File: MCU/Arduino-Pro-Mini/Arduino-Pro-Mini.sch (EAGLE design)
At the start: 19 parts, among them Q1 8/16/20MHz, U1 ATMEGA328

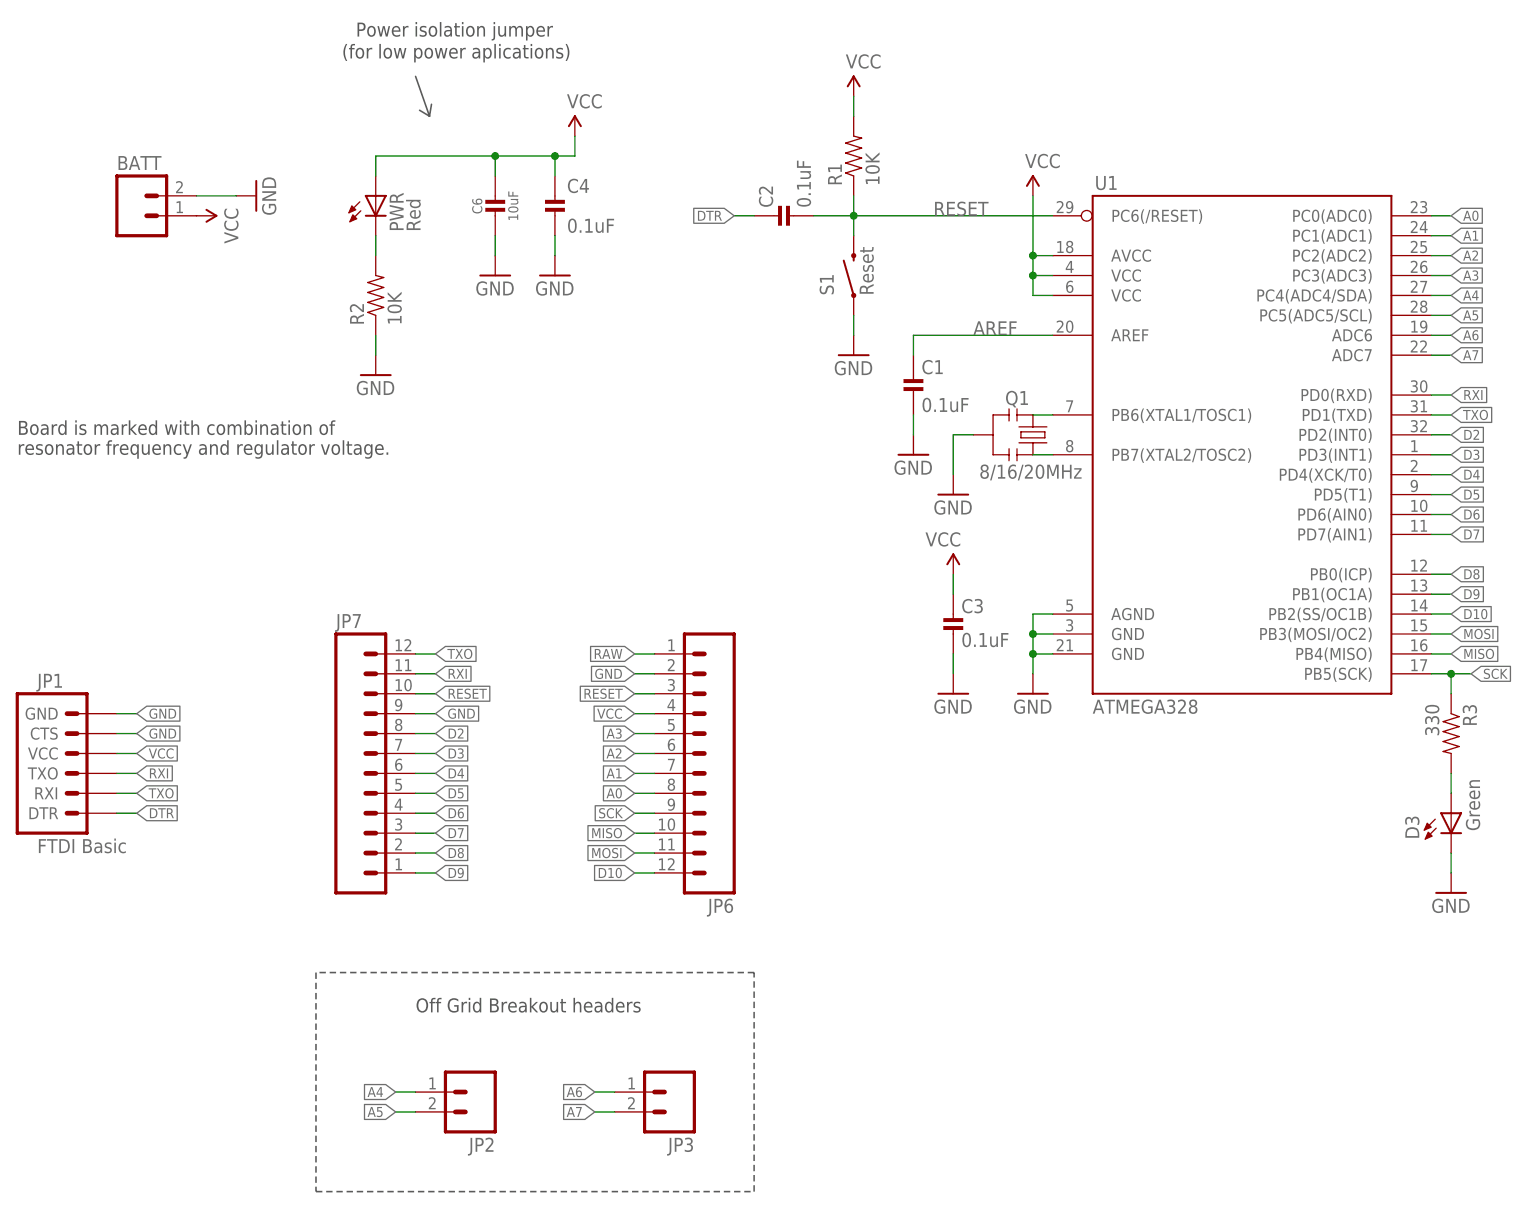
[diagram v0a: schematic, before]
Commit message: pro mini board route
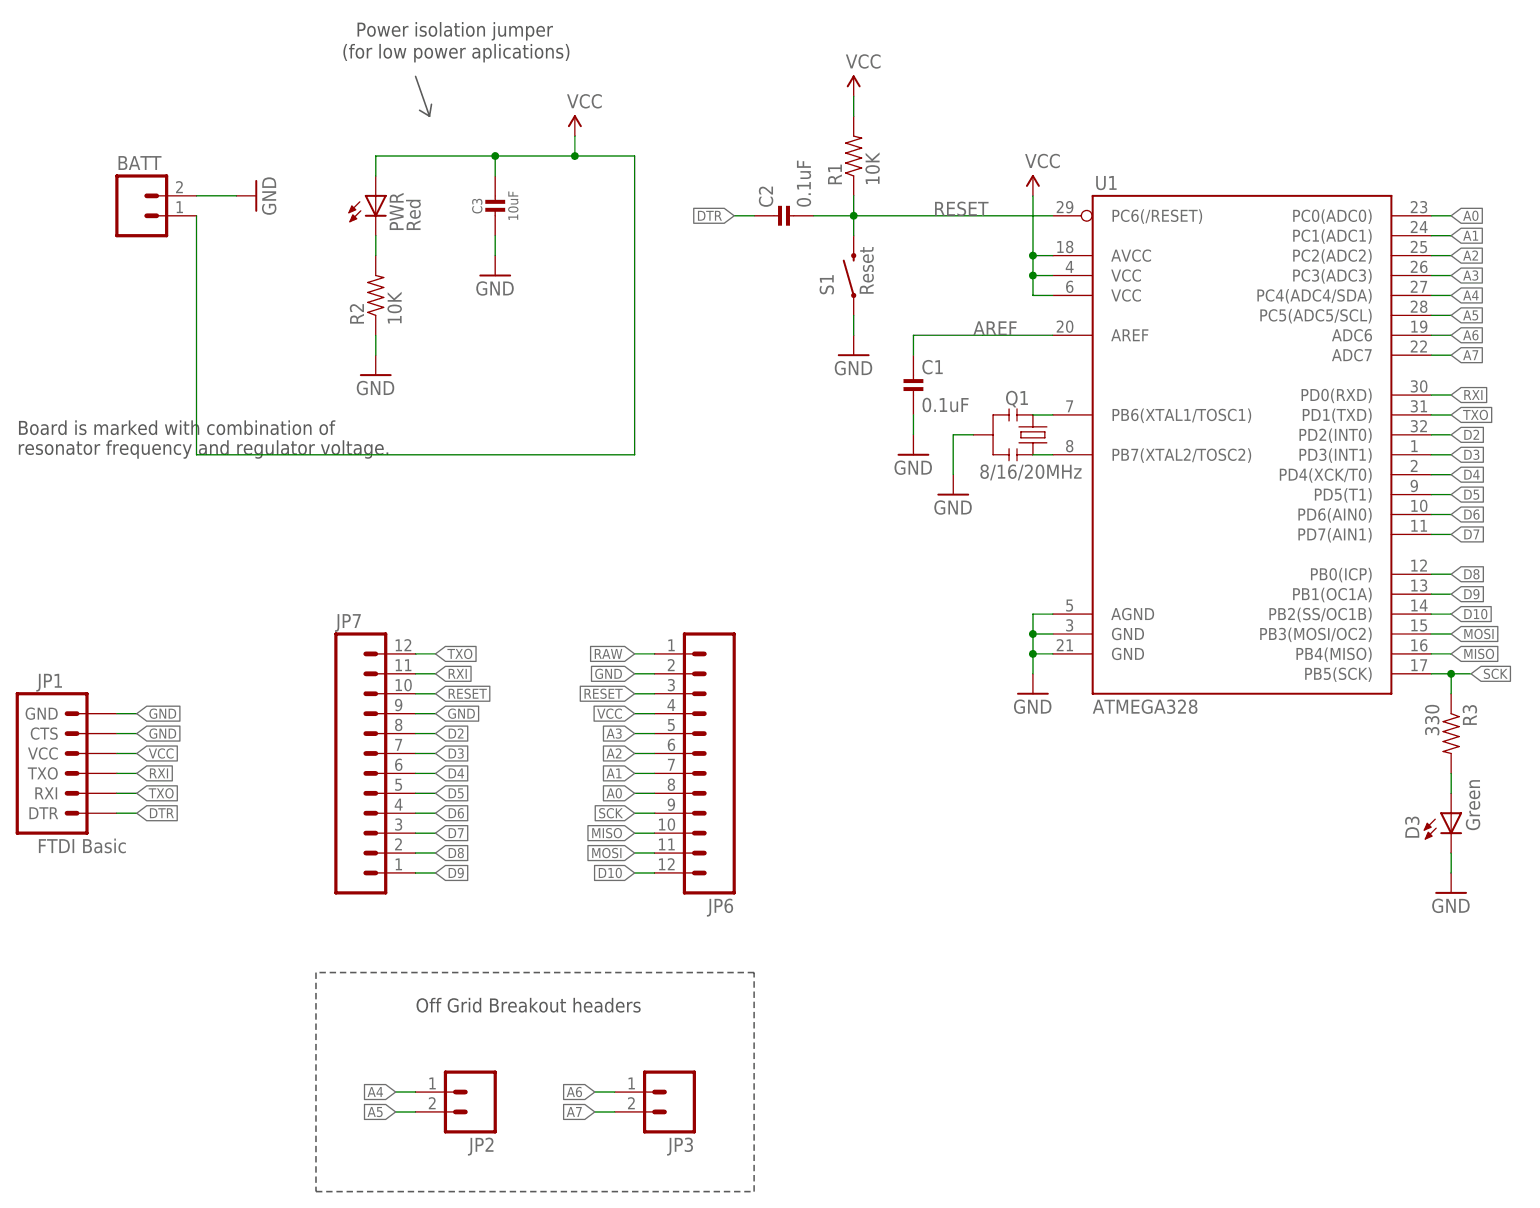
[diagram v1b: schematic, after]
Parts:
- removed C4: 0.1uF, Scott-Electrical:CAP_CERAMIC_0603
- removed C6: 10uF, Scott-Electrical:CAP_CERAMIC_0805
- C3: value 0.1uF -> 10uF; device Scott-Electrical:CAP_CERAMIC_0603 -> Scott-Electrical:CAP_CERAMIC_0805
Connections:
- removed net 3.3V: BATT.1
- net GND: now also C3.2; no longer C3.1, C4.2, C6.2
- net VCC: now also BATT.1, C3.1; no longer C3.2, C4.1, C6.1
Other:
- moved on the sheet: C3
